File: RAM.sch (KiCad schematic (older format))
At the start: 13 parts, among them U71 74LS245, U72 74LS173, U73 74LS173, U74 74LS245, U75 74LS173, U76 74LS173, U77 74HC04, U78 74HC00, U79 AT28C256, U80 AT28C256, U81 AS6C62256A, U82 AS6C62256A, U83 74HC04

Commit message: fixed almost all errors
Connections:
- no-connect marks 20 -> 2
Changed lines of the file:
@@
 Text HLabel 1350 2400 0    50   3State ~ 0
 Bus15
-NoConn ~ 22700 900
-NoConn ~ 22700 1000
-NoConn ~ 22700 1100
-NoConn ~ 22700 1200
-NoConn ~ 22700 1300
-NoConn ~ 22700 1400
-NoConn ~ 22700 1500
-NoConn ~ 22700 1600
-NoConn ~ 22700 1700
-NoConn ~ 22700 1800
-NoConn ~ 22700 1900
-NoConn ~ 22700 2000
-NoConn ~ 22700 2100
-NoConn ~ 22700 2200
-NoConn ~ 22700 2300
-NoConn ~ 22700 2400
 Connection ~ 9500 2400
 Connection ~ 8250 1700
@@
 	1    0    0    -1
 $EndComp
-NoConn ~ 10250 8150
-NoConn ~ 10250 8650
 Wire Wire Line
 	6550 5100 9800 5100

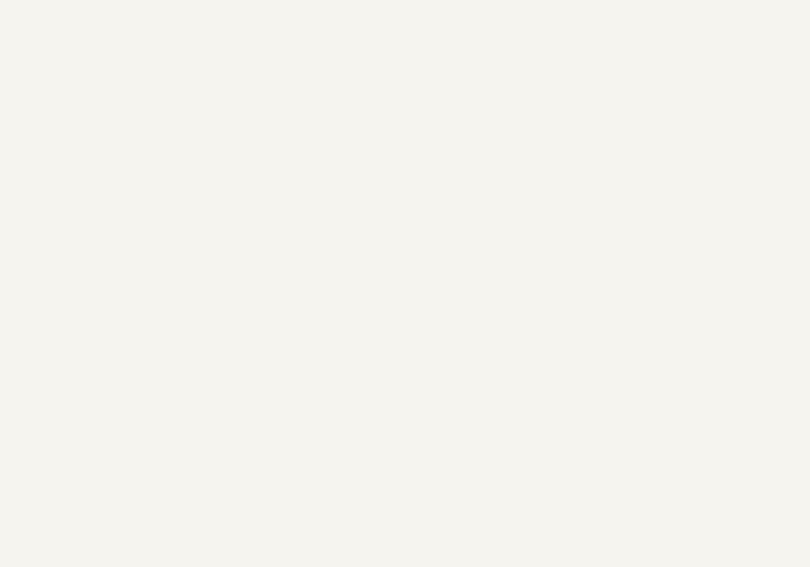
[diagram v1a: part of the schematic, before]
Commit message: added power caps
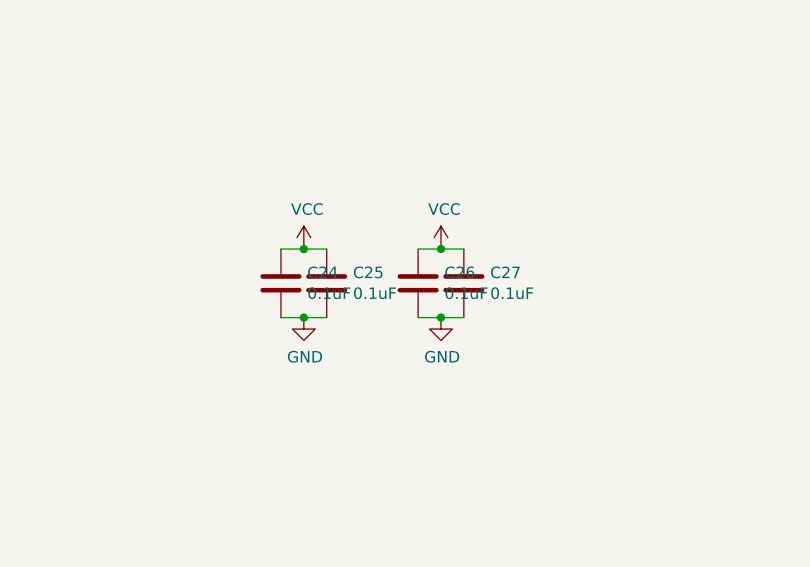
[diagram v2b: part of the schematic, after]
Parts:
- added C24, C25, C26, C27: 0.1uF, Capacitor_THT:CP_Axial_L10.0mm_D4.5mm_P15.00mm_Horizontal, symbol Device:C
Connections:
- net labels added: VCC
- wire segments 517 -> 525
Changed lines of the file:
@@
 $Descr A2 23386 16535
 encoding utf-8
-Sheet 20 21
+Sheet 19 21
 Title ""
 Date ""
@@
 Wire Wire Line
 	1500 10700 16250 10700
+$Comp
+L 16bitCpu-rescue:VCC-power #PWR?
+U 1 1 5FCB0FE2
+P 20400 4800
+AR Path="/5FCB0FE2" Ref="#PWR?"  Part="1"
+AR Path="/5F681977/5FCB0FE2" Ref="#PWR0277"  Part="1"
+F 0 "#PWR0277" H 20400 4650 50  0001 C CNN
+F 1 "VCC" H 20415 4973 50  0000 C CNN
+F 2 "" H 20400 4800 50  0001 C CNN
+F 3 "" H 20400 4800 50  0001 C CNN
+	1    20400 4800
+	1    0    0    -1
+$EndComp
+$Comp
+L 16bitCpu-rescue:GND-power #PWR?
+U 1 1 5FCB0FE8
+P 20400 5100
+AR Path="/5FCB0FE8" Ref="#PWR?"  Part="1"
+AR Path="/5F75E433/5FCB0FE8" Ref="#PWR?"  Part="1"
+AR Path="/5F681977/5FCB0FE8" Ref="#PWR0278"  Part="1"
+F 0 "#PWR0278" H 20400 4850 50  0001 C CNN
+F 1 "GND" H 20405 4927 50  0000 C CNN
+F 2 "" H 20400 5100 50  0001 C CNN
+F 3 "" H 20400 5100 50  0001 C CNN
+	1    20400 5100
+	1    0    0    -1
+$EndComp
+Wire Wire Line
+	20400 4800 20500 4800
+Wire Wire Line
+	20500 5100 20400 5100
+$Comp
+L Device:C C?
+U 1 1 5FCB0FF0
+P 20300 4950
+AR Path="/5F75E433/5FCB0FF0" Ref="C?"  Part="1"
+AR Path="/5F681977/5FCB0FF0" Ref="C24"  Part="1"
+F 0 "C24" H 20415 4996 50  0000 L CNN
+F 1 "0.1uF" H 20415 4905 50  0000 L CNN
+F 2 "Capacitor_THT:CP_Axial_L10.0mm_D4.5mm_P15.00mm_Horizontal" H 20338 4800 50  0001 C CNN
+F 3 "" H 20300 4950 50  0001 C CNN
+	1    20300 4950
+	1    0    0    -1
+$EndComp
+Wire Wire Line
+	20400 4800 20300 4800
+Connection ~ 20400 4800
+Wire Wire Line
+	20300 5100 20400 5100
+Connection ~ 20400 5100
+$Comp
+L Device:C C?
+U 1 1 5FCB0FFA
+P 20500 4950
+AR Path="/5F75E433/5FCB0FFA" Ref="C?"  Part="1"
+AR Path="/5F681977/5FCB0FFA" Ref="C25"  Part="1"
+F 0 "C25" H 20615 4996 50  0000 L CNN
+F 1 "0.1uF" H 20615 4905 50  0000 L CNN
+F 2 "Capacitor_THT:CP_Axial_L10.0mm_D4.5mm_P15.00mm_Horizontal" H 20538 4800 50  0001 C CNN
+F 3 "" H 20500 4950 50  0001 C CNN
+	1    20500 4950
+	1    0    0    -1
+$EndComp
+$Comp
+L 16bitCpu-rescue:VCC-power #PWR?
+U 1 1 5FCF0944
+P 21000 4800
+AR Path="/5FCF0944" Ref="#PWR?"  Part="1"
+AR Path="/5F681977/5FCF0944" Ref="#PWR0279"  Part="1"
+F 0 "#PWR0279" H 21000 4650 50  0001 C CNN
+F 1 "VCC" H 21015 4973 50  0000 C CNN
+F 2 "" H 21000 4800 50  0001 C CNN
+F 3 "" H 21000 4800 50  0001 C CNN
+	1    21000 4800
+	1    0    0    -1
+$EndComp
+$Comp
+L 16bitCpu-rescue:GND-power #PWR?
+U 1 1 5FCF094A
+P 21000 5100
+AR Path="/5FCF094A" Ref="#PWR?"  Part="1"
+AR Path="/5F75E433/5FCF094A" Ref="#PWR?"  Part="1"
+AR Path="/5F681977/5FCF094A" Ref="#PWR0280"  Part="1"
+F 0 "#PWR0280" H 21000 4850 50  0001 C CNN
+F 1 "GND" H 21005 4927 50  0000 C CNN
+F 2 "" H 21000 5100 50  0001 C CNN
+F 3 "" H 21000 5100 50  0001 C CNN
+	1    21000 5100
+	1    0    0    -1
+$EndComp
+Wire Wire Line
+	21000 4800 21100 4800
+Wire Wire Line
+	21100 5100 21000 5100
+$Comp
+L Device:C C?
+U 1 1 5FCF0952
+P 20900 4950
+AR Path="/5F75E433/5FCF0952" Ref="C?"  Part="1"
+AR Path="/5F681977/5FCF0952" Ref="C26"  Part="1"
+F 0 "C26" H 21015 4996 50  0000 L CNN
+F 1 "0.1uF" H 21015 4905 50  0000 L CNN
+F 2 "Capacitor_THT:CP_Axial_L10.0mm_D4.5mm_P15.00mm_Horizontal" H 20938 4800 50  0001 C CNN
+F 3 "" H 20900 4950 50  0001 C CNN
+	1    20900 4950
+	1    0    0    -1
+$EndComp
+Wire Wire Line
+	21000 4800 20900 4800
+Connection ~ 21000 4800
+Wire Wire Line
+	20900 5100 21000 5100
+Connection ~ 21000 5100
+$Comp
+L Device:C C?
+U 1 1 5FCF095C
+P 21100 4950
+AR Path="/5F75E433/5FCF095C" Ref="C?"  Part="1"
+AR Path="/5F681977/5FCF095C" Ref="C27"  Part="1"
+F 0 "C27" H 21215 4996 50  0000 L CNN
+F 1 "0.1uF" H 21215 4905 50  0000 L CNN
+F 2 "Capacitor_THT:CP_Axial_L10.0mm_D4.5mm_P15.00mm_Horizontal" H 21138 4800 50  0001 C CNN
+F 3 "" H 21100 4950 50  0001 C CNN
+	1    21100 4950
+	1    0    0    -1
+$EndComp
 $EndSCHEMATC

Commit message: added display
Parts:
- renumbered U71 to U64, U72 to U65, U73 to U66, U74 to U67, U75 to U68, U76 to U69, U77 to U70, U78 to U71, U79 to U72, U80 to U73, U81 to U74, U82 to U75, U83 to U76

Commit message: clean up
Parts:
- renumbered U64 to U66, U65 to U67, U66 to U68, U67 to U69, U68 to U70, U69 to U71, U70 to U72, U71 to U73, U72 to U74, U73 to U75, U74 to U76, U75 to U77, U76 to U78
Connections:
- wire segments 525 -> 509
